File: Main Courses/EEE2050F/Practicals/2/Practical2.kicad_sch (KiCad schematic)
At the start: 0 parts

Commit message: Complete schematics A and E
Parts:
- added IC1, IC4: 4071, symbol 4xxx:4071
- added IC2: 4049, symbol 4xxx:4049
- added IC3: 4081, symbol 4xxx:4081
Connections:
- new net: IC3.2, IC4.3
- new net: IC2.4, IC4.6
- new net: IC1.4, IC3.8
- new net: IC1.3, IC1.5
- new net: IC4.4, IC4.9
- new net: IC1.13, IC1.9, IC2.2, IC4.5
- new net: IC3.4, IC3.9
- new net: IC1.11, IC3.1
- new net: IC3.3, IC4.8
- new net: IC3.5, IC4.10
- new net: IC1.10, IC1.12
- new net A: IC1.1, IC2.3
- new net B: IC1.2, IC2.5, IC4.1
- new net C: IC1.6, IC1.8, IC3.6, IC4.2
- new net Y: IC3.10
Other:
- added sheet E (Practical2_E.kicad_sch)
- company: (none) -> Adam Foflonker (FFLADA001)
- title: (none) -> Unsimplified boolean equation

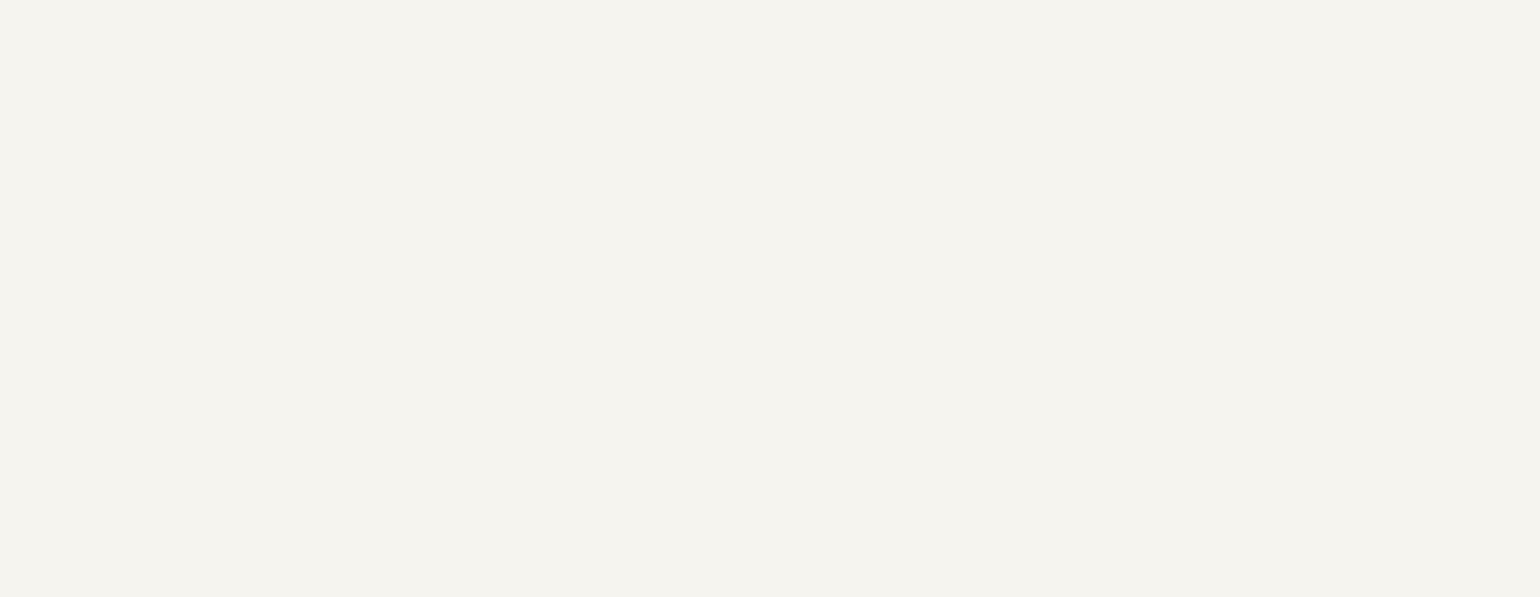
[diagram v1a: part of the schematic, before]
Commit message: Add power supply circuit to schematic
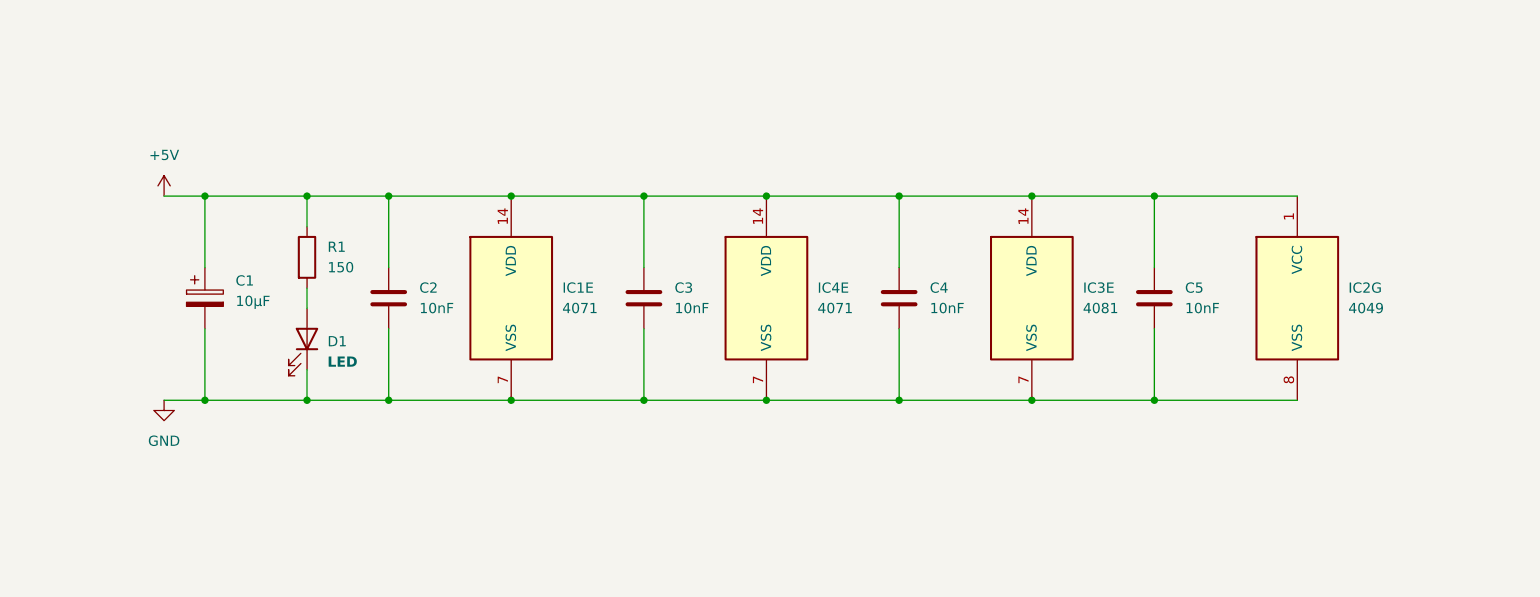
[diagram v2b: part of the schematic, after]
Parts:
- added C1: 10µF, symbol Device:C_Polarized
- added C2, C3, C4, C5: 10nF, symbol Device:C
- added D1: LED, symbol Device:LED
- added unit 5 of IC1
- added unit 7 of IC2
- added unit 5 of IC3
- added unit 5 of IC4
- added R1: 150, symbol Device:R
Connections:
- new net: D1.2 (A), R1.2
- new net +5V: C1.1, C2.1, C3.1, C4.1, C5.1, IC1.14 (VDD), IC2.1 (VCC), IC3.14 (VDD), IC4.14 (VDD), R1.1
- new net GND: C1.2, C2.2, C3.2, C4.2, C5.2, D1.1 (K), IC1.7 (VSS), IC2.8 (VSS), IC3.7 (VSS), IC4.7 (VSS)

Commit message: Add unused gates to schematic
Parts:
- added unit 3 of IC2
- added unit 4 of IC2
- added unit 4 of IC3
- added unit 4 of IC4
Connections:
- net GND: now also IC2.7, IC2.9, IC3.12, IC3.13, IC4.12, IC4.13
- no-connect marks 0 -> 4

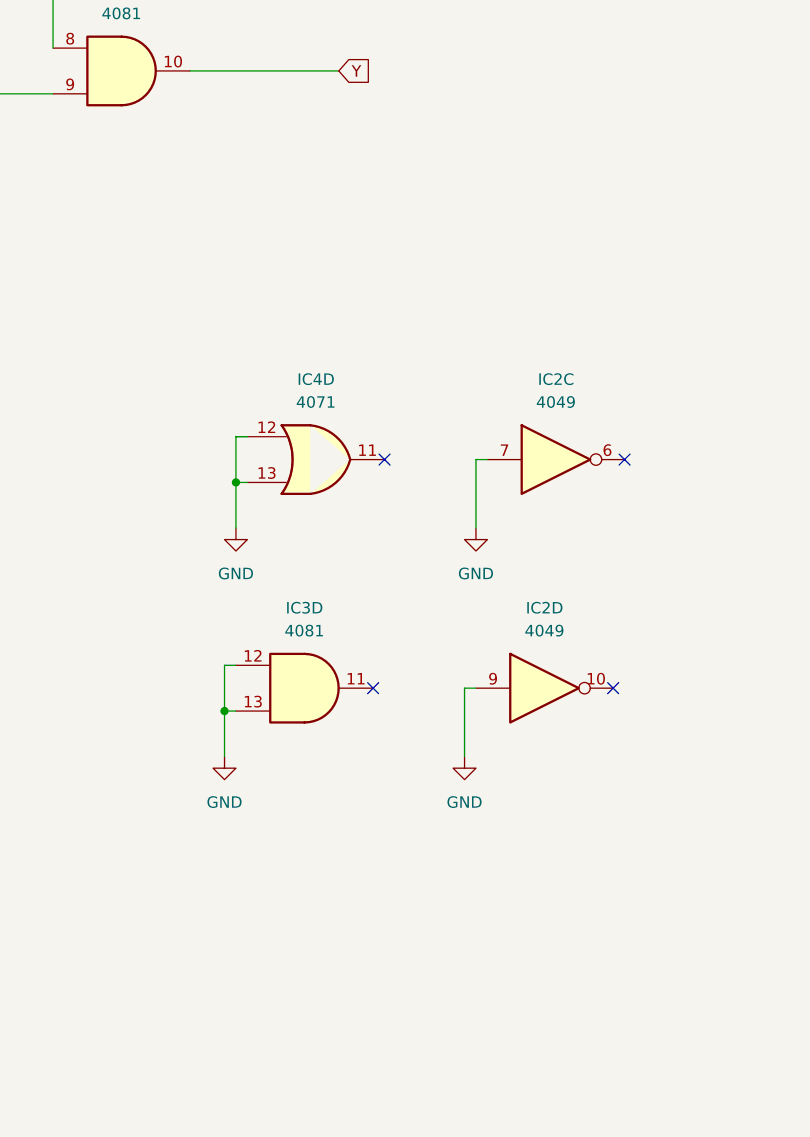
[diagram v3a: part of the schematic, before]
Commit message: Add missing CD4049 gates
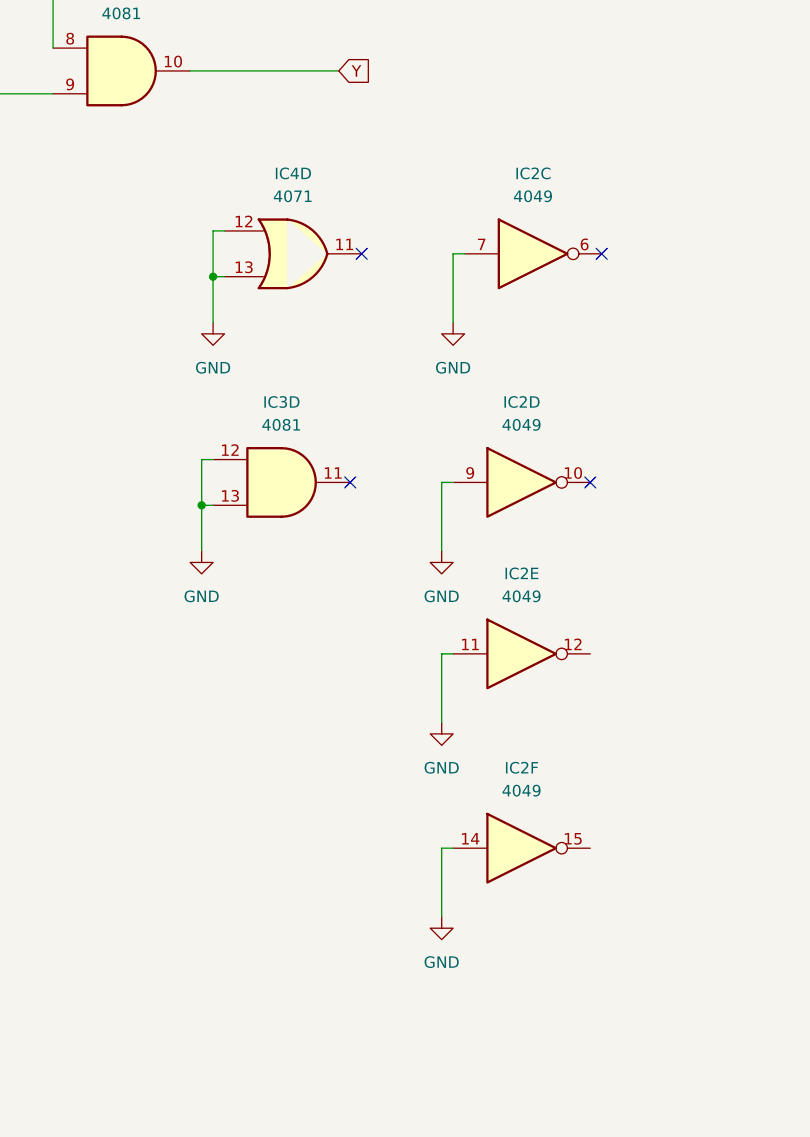
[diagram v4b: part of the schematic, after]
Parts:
- added unit 5 of IC2
- added unit 6 of IC2
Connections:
- net GND: now also IC2.11, IC2.14
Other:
- moved on the sheet: IC2C, IC2D, IC3D, IC4D

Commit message: Complete schematic 3
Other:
- added sheet I (Practical2_I.kicad_sch)
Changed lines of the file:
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@@
+	)
+	(sheet
+		(at 2.54 405.13)
+		(size 299.72 163.83)
+		(exclude_from_sim no)
+		(in_bom yes)
+		(on_board yes)
+		(dnp no)
+		(fields_autoplaced yes)
+		(stroke
+			(width 0.1524)
+			(type solid)
+		)
+		(fill
+			(color 0 0 0 0.0000)
+		)
+		(property "Sheetname" "I"
+			(at 2.54 404.4184 0)
+			(effects
+				(font
+					(size 1.27 1.27)
+				)
+				(justify left bottom)
+			)
+		)
+		(property "Sheetfile" "Practical2_I.kicad_sch"
+			(at 2.54 569.5446 0)
+			(effects
+				(font
+					(size 1.27 1.27)
+				)
+				(justify left top)
+			)
+		)
+		(instances
+			(project "Practical2"
+				(path "/ace74c6e-23b9-4de0-b351-789173787281"
+					(page "3")
+				)
+			)
+		)
 	)
 	(sheet
